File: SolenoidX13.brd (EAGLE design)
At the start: 25.4 x 25.4 mm, 0 parts

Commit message: owo
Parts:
- added C1, C10, C2, C7, C8, C9: 4.7uF, SparkFun-Capacitors:0603
- added C11: 0.1uF, SparkFun-Capacitors:0603
- added C3, C4: 100nF, SparkFun-Capacitors:0603
- added C5: 0.01uF, SparkFun-Capacitors:0603
- added C6: 1uF, SparkFun-Capacitors:0603
- added D1, D2, D4: (no value), SparkFun-LED:LED-0603
- added J1, J3, J4: (no value), SparkFun-Connectors:1X02
- added R1, R2, R3: 1k, SparkFun-Resistors:0603
- added R10, R11: 60, SparkFun-Resistors:0603
- added R4, R6, R7: (no value), SparkFun-Resistors:0603
- added RESET: (no value), DiscreteComponents:SW_2512
- added SV1: (no value), con-lsta:FE05-1
- added U$3: STM32F042K6T6, PI_Shield_Library:STM32F042K6T6
- added U$8: TCAN337D, PI_Shield_Library:TCAN337D
- added U1: ULN2003V12, ULN2003V12:ULN2003V12
- added Y1: ECS-80-S-4X, ECS-80-S-4X:XTAL_ECS-80-S-4X
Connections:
- new net +3V3: C1.1, C10.1, C2.1, C3.1, C4.1, C5.1, C6.1, R2.2, R6.2, SV1.5, U$3.VDD, U$3.VDDA, U$3.VDDIO2, U$8.VCC
- new net 12V: J3.2, R4.2, U1.9
- new net 3.3V: J1.2
- new net CAN_H: J4.2, R10.2, U$8.CANH
- new net CAN_L: J4.1, R11.1, U$8.CANL
- new net CAN_RX: U$3.PA11, U$8.RXD
- new net CAN_TX: U$3.PA12, U$8.TXD
- new net GND: C1.2, C10.2, C11.1, C2.2, C3.2, C4.2, C5.2, C6.2, C7.2, C8.2, C9.2, D1.C, D2.C, D4.C, J1.1, J3.1, RESET.1, SV1.3, U$3.PB8-BOOT0, U$3.VSS, U$3.VSS1, U$8.GND, U1.8
- new net GPIO0: U$3.PB7
- new net GPIO1: U$3.PB6, U1.4
- new net GPIO10: U$3.PA5, U1.3
- new net GPIO11: U$3.PA6, U1.2
- new net GPIO12: U$3.PA7, U1.1
- new net GPIO13: U$3.PA8
- new net GPIO14: U$3.PA9
- new net GPIO15: U$3.PA10
- new net GPIO2: U$3.PB4, U1.5
- new net GPIO3: U$3.PB3, U1.6
- new net GPIO8: U$3.PA3
- new net GPIO9: U$3.PA4
- new net LED: R7.2, U$3.PA15
- new net N$1: C9.1, R1.1, Y1.2
- new net N$2: C8.1, R3.1, Y1.1
- new net N$24: D1.A, R7.1
- new net N$25: D4.A, R4.1
- new net N$27: D2.A, R6.1
- new net N$5: C11.2, R10.1, R11.2
- new net NRST: SV1.1
- new net NRST1: C7.1, R2.1, RESET.2, U$3.NRST
- new net OSC_IN: R3.2, U$3.PF0-OSC_IN
- new net OSC_OUT: R1.2, U$3.PF1-OSC_OUT
- new net SOL1_1: U1.16
- new net SOL2_1: U1.15
- new net SOL3_1: U1.14
- new net SOL4_1: U1.13
- new net SOL5_1: U1.12
- new net SOL6_1: U1.11
- new net SWCLK: SV1.4, U$3.PA14
- new net SWDIO: SV1.2, U$3.PA13
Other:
- board size 25.4 x 25.4 mm -> 35.6 x 30.5 mm

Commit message: owo?
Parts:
- removed C8, C9: 4.7uF, SparkFun-Capacitors:0603
- removed R4, R6: (no value), SparkFun-Resistors:0603
- removed Y1: ECS-80-S-4X, ECS-80-S-4X:XTAL_ECS-80-S-4X
- R1: value 1k -> 680
- R10, R11: value 60 -> 1k
- R3: value 1k -> 82
- moved R1 39.4 mm to (-18.8, -25.4)
- moved R3 31.2 mm to (-19.1, -22.1)
- moved U$3 5.86 mm to (22.9, 14.2)
- moved U1 2.59 mm to (17.3, 10.9)
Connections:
- removed net GPIO2: U$3.PB4, U1.5
- removed net GPIO3: U$3.PB3, U1.6
- removed net N$1: C9.1, R1.1, Y1.2
- removed net N$2: C8.1, R3.1, Y1.1
- removed net OSC_IN: R3.2, U$3.PF0-OSC_IN
- removed net OSC_OUT: R1.2, U$3.PF1-OSC_OUT
- new net GPIO4: U1.4
- new net GPIO5: U$3.PA2, U1.2, U1.5
- new net GPIO6: U$3.PA3, U1.3, U1.6
- net +3V3: now also R3.2; no longer R6.2
- net 12V: now also R1.2; no longer R4.2
- net GND: no longer C8.2, C9.2
- net GPIO0: now also U$3.PA1; no longer U$3.PB7
- net GPIO1: now also U$3.PA0, U1.1; no longer U$3.PB6, U1.4
- net GPIO10: now also U$3.PA7; no longer U$3.PA5, U1.3
- net GPIO11: now also U$3.PB0; no longer U$3.PA6, U1.2
- net GPIO12: now also U$3.PB1; no longer U$3.PA7, U1.1
- net GPIO8: now also U$3.PA5; no longer U$3.PA3
- net GPIO9: now also U$3.PA6; no longer U$3.PA4
- net N$25: now also R1.1; no longer R4.1
- net N$27: now also R3.1; no longer R6.1

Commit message: hi
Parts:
- moved U1 0.76 mm to (16.5, 10.9), flipped to the bottom, turned to 0 degrees
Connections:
- removed net GPIO10: U$3.PA7
- removed net GPIO11: U$3.PB0
- removed net GPIO12: U$3.PB1
- removed net GPIO13: U$3.PA8
- removed net GPIO14: U$3.PA9
- removed net GPIO15: U$3.PA10
- removed net GPIO8: U$3.PA5
- removed net GPIO9: U$3.PA6
- new net GPIO2: U$3.PA2, U1.2
- new net GPIO3: U$3.PA3, U1.3
- net GPIO0: now also U$3.PA0; no longer U$3.PA1
- net GPIO1: now also U$3.PA1; no longer U$3.PA0
- net GPIO4: now also U$3.PA4
- net GPIO5: now also U$3.PA5; no longer U$3.PA2, U1.2
- net GPIO6: now also U$3.PA6; no longer U$3.PA3, U1.3

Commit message: board is done lol
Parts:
- removed J3, J4: (no value), SparkFun-Connectors:1X02
- J1: value (none) -> SAMTEC-CLT-111-01-X-DJ; device SparkFun-Connectors:1X02 -> SAMTEC-CLT-111-01-X-D:SAMTEC-CLT-111-01-X-D
- moved R3 65.7 mm to (25.0, 26.6), flipped to the bottom
- moved R2 57.6 mm to (31.2, 25.1), flipped to the bottom
- moved R1 56.2 mm to (14.7, 19.7), turned to 270 degrees
- moved RESET 53.6 mm to (33.3, 22.9), turned to 90 degrees
- moved R7 51.9 mm to (33.3, 17.5), flipped to the bottom, turned to 180 degrees
- moved C10 50.4 mm to (2.18, 20.4), turned to 180 degrees
- moved D1 49.1 mm to (33.3, 17.5)
- moved C7 48.7 mm to (31.2, 26.7), flipped to the bottom
- moved SV1 45.2 mm to (33.3, 9.40), turned to 270 degrees
- moved R10 36.9 mm to (17.0, 8.89), flipped to the bottom, turned to 270 degrees
- moved J1 34.7 mm to (7.72, 15.7), turned to 270 degrees
- moved R11 31.7 mm to (17.0, 5.59), flipped to the bottom, turned to 270 degrees
- moved D2 29.4 mm to (33.2, 27.7)
- moved D4 29.2 mm to (33.2, 29.4)
- moved C11 28.7 mm to (20.1, 3.81), flipped to the bottom
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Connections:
- removed net 3.3V: J1.2
- new net ALERT1: J1.18, U$3.PB4
- new net ALERT2: J1.17, U$3.PB3
- new net C2_1: J1.16, U$3.PB0
- new net C2_2: J1.15, U$3.PB1
- new net CLK: J1.20, U$3.PA9
- new net DATA: J1.22, U$3.PA10
- new net GPIO7: U$3.PA7
- net +3V3: now also J1.6
- net 12V: now also J1.11; no longer J3.2
- net CAN_H: now also J1.19; no longer J4.2
- net CAN_L: now also J1.21; no longer J4.1
- net GND: now also J1.10, J1.12, J1.4, J1.8; no longer J1.1, J3.1
- net SOL1_1: now also J1.2
- net SOL2_1: now also J1.1
- net SOL3_1: now also J1.3
- net SOL4_1: now also J1.5
- net SOL5_1: now also J1.7
- net SOL6_1: now also J1.9
- net SWCLK: now also U$3.PA13; no longer U$3.PA14
- net SWDIO: now also U$3.PA14; no longer U$3.PA13
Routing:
- net +3V3: track 0.00 -> 83.2 mm, vias 0 -> 4
- net DATA: track 0.00 -> 29.7 mm
- net ALERT1: track 0.00 -> 26.3 mm, vias 0 -> 1
- net N$25: track 0.00 -> 24.9 mm
- net ALERT2: track 0.00 -> 22.9 mm, vias 0 -> 1
- net CLK: track 0.00 -> 21.9 mm
- net C2_1: track 0.00 -> 17.0 mm
- net NRST1: track 0.00 -> 13.9 mm, vias 0 -> 1
- net C2_2: track 0.00 -> 13.6 mm
- net N$5: track 0.00 -> 12.6 mm
- net CAN_TX: track 0.00 -> 11.0 mm, vias 0 -> 1
- net CAN_RX: track 0.00 -> 11.0 mm, vias 0 -> 1
- net SWCLK: track 0.00 -> 10.8 mm
- net CAN_L: track 0.00 -> 9.85 mm
- net CAN_H: track 0.00 -> 9.85 mm
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- added copper zone on layer 1, net GND
- added copper zone on layer 16, net GND
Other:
- board text added: "12V 3.3V"
- board text added: "STM"

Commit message: lol
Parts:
- removed RESET: (no value), DiscreteComponents:SW_2512
- added U$1: (no value), Push button - FSM2JMTR:DISCRETECOMPONENTS_SW_2512
- moved C10 27.7 mm to (22.8, 1.93), flipped to the bottom, turned to 270 degrees
- moved C4 20.0 mm to (17.6, 14.6), turned to 90 degrees
- moved C1 19.7 mm to (19.1, 17.6), flipped to the bottom, turned to 270 degrees
- moved C3 19.1 mm to (20.5, 17.6), flipped to the bottom, turned to 270 degrees
- moved C5 16.8 mm to (16.7, 17.0), flipped to the bottom, turned to 0 degrees
- moved C2 16.0 mm to (16.1, 14.6), turned to 90 degrees
- moved C6 16.0 mm to (16.7, 18.5)
- moved R7 13.6 mm to (19.9, 15.2), turned to 0 degrees
- moved C7 11.0 mm to (24.7, 17.8)
- moved D4 9.56 mm to (25.0, 24.5)
- moved D1 9.45 mm to (25.0, 22.1)
- moved D2 9.30 mm to (25.0, 23.3)
- moved SV1 8.92 mm to (24.9, 6.35)
- moved U$8 8.75 mm to (16.3, 1.52)
- moved R2 8.75 mm to (24.7, 19.4)
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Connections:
- net GND: now also U$1.1; no longer RESET.1
- net NRST1: now also U$1.2; no longer RESET.2
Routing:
- net DATA: track 29.7 -> 2.13 mm
- net CLK: track 21.9 -> 0.00 mm
- net +3V3: track 83.2 -> 61.9 mm, vias 4 -> 3
- net SWCLK: track 10.8 -> 0.54 mm
- net N$5: track 12.6 -> 3.08 mm
- net N$24: track 2.34 -> 9.08 mm
- net N$25: track 24.9 -> 20.1 mm
- net GPIO1: track 6.47 -> 2.84 mm
- net GPIO2: track 4.54 -> 0.95 mm, vias 1 -> 0
- net GPIO3: track 3.38 -> 0.00 mm, vias 1 -> 0
- net GPIO4: track 2.97 -> 0.00 mm, vias 1 -> 0
- net GPIO6: track 2.93 -> 0.00 mm, vias 1 -> 0
- net ALERT1: track 26.3 -> 23.4 mm
- net C2_1: track 17.0 -> 14.1 mm
- net C2_2: track 13.6 -> 10.7 mm
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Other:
- board size 35.6 x 30.5 mm -> 27.4 x 25.4 mm

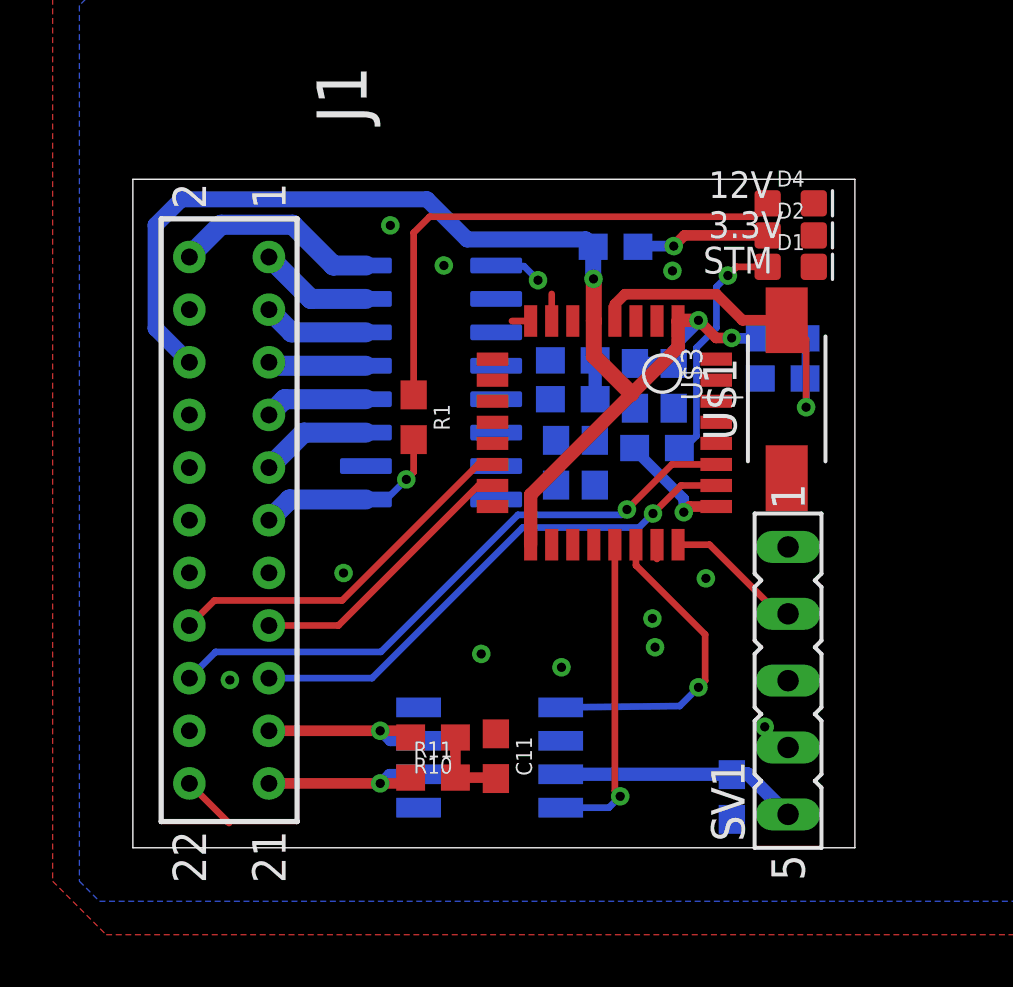
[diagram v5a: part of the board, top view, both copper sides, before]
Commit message: it is smol now, cap gulag is gone, reset switch updated, clt part added to parts lib
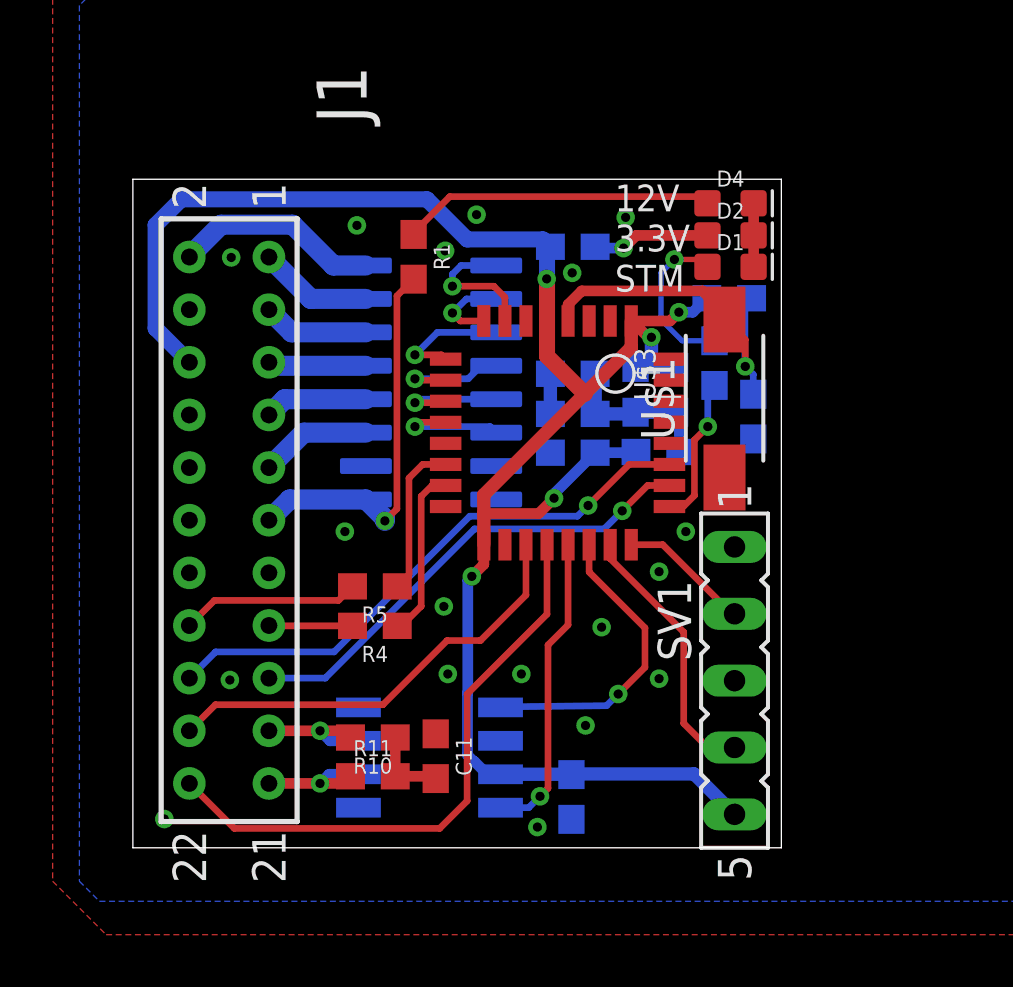
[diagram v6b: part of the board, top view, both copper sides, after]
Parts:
- added R4, R5: 4.7k, SparkFun-Resistors:0603
- moved C10 6.10 mm to (16.7, 1.93)
- moved R1 6.10 mm to (10.7, 22.5)
- moved R7 3.90 mm to (22.1, 18.4), turned to 270 degrees
- moved R2 2.54 mm to (22.7, 20.9)
- moved C4 2.45 mm to (20.0, 15.0), turned to 180 degrees
- moved U$1 2.36 mm to (22.5, 17.1)
- moved R11 2.29 mm to (9.12, 2.72)
- moved D1 2.29 mm to (22.7, 22.1)
- moved D2 2.29 mm to (22.7, 23.3)
- moved D4 2.29 mm to (22.7, 24.5)
- moved C11 2.29 mm to (11.5, 3.48)
- moved R10 2.29 mm to (9.12, 4.19)
- moved U$8 2.29 mm to (14.0, 1.52)
- moved SV1 2.03 mm to (22.9, 6.35)
- moved C7 1.83 mm to (23.6, 16.4), turned to 270 degrees
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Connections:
- new net N$1: R4.1, U$3.PB1
- new net N$2: R5.1, U$3.PB0
- net C2_1: now also R5.2; no longer U$3.PB0
- net C2_2: now also R4.2; no longer U$3.PB1
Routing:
- net DATA: track 2.13 -> 22.7 mm
- net CLK: track 0.00 -> 16.8 mm
- net +3V3: track 61.9 -> 77.3 mm, vias 3 -> 5
- net SWCLK: track 0.54 -> 10.3 mm
- net GND: track 0.00 -> 8.60 mm, vias 11 -> 18
- net N$25: track 20.1 -> 11.9 mm
- net C2_2: track 10.7 -> 3.18 mm
- net 12V: track 7.49 -> 14.8 mm
- net C2_1: track 14.1 -> 6.81 mm
- net N$1: track 0.00 -> 6.49 mm
- net N$2: track 0.00 -> 5.91 mm
- net GPIO3: track 0.00 -> 4.68 mm, vias 0 -> 1
- net GPIO4: track 0.00 -> 4.48 mm, vias 0 -> 1
- net GPIO6: track 0.00 -> 4.42 mm, vias 0 -> 1
- net GPIO5: track 0.07 -> 4.38 mm, vias 0 -> 1
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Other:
- board size 27.4 x 25.4 mm -> 24.6 x 25.4 mm
- board text added: "12V 3.3V STM"
- board text removed: "12V 3.3V"
- board text removed: "STM"

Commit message: ready for design review tbh
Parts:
- moved C4 10.6 mm to (11.4, 8.74), turned to 0 degrees
- moved C2 7.16 mm to (11.4, 10.2)
- moved R3 0.59 mm to (16.2, 22.6), flipped to the top, turned to 180 degrees
- moved C5 0.31 mm to (16.4, 16.5)
- moved C7 0.31 mm to (23.3, 16.4)
- moved R2 0.31 mm to (22.4, 20.9)
- moved R7 0.31 mm to (21.8, 18.4)
- moved U$1 0.31 mm to (22.2, 17.1)
- moved U$3 0.31 mm to (13.0, 20.0)
- moved U1 0.31 mm to (11.0, 17.7)
- moved R10 0.31 mm to (8.81, 4.22)
- moved SV1 0.31 mm to (22.6, 6.38)
- moved C10 0.31 mm to (16.4, 1.96)
- moved C11 0.31 mm to (11.2, 3.51)
- moved J1 0.31 mm to (3.35, 12.5)
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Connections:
- removed net NRST1: C7.1, R2.1, U$1.2, U$3.NRST
- net NRST: now also C7.1, R2.1, U$1.2, U$3.NRST
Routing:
- net NRST: track 0.00 -> 19.6 mm, vias 0 -> 1
- net NRST1: track 13.4 -> 0.00 mm, vias 1 -> 0
- net +3V3: track 77.3 -> 71.8 mm, vias 5 -> 4
- net GND: track 8.60 -> 7.00 mm, vias 18 -> 23
- net N$27: track 4.49 -> 4.79 mm, vias 1 -> 0
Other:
- board size 24.6 x 25.4 mm -> 24.3 x 25.4 mm
- board text added: "ROV X13 Solenoid 12/04/2020 Erin Park Katherine Sandys Grant Geyer"
